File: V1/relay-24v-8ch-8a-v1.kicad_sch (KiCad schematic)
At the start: 44 parts, among them J1 DB141V-2.54-6P, J2 DB141V-2.54-6P, J3 DB142V-5.08-8P, J4 DB142V-5.08-8P, K1 G5Q-1A4-DC24V, K2 G5Q-1A4-DC24V, K3 G5Q-1A4-DC24V, K4 G5Q-1A4-DC24V, K5 G5Q-1A4-DC24V, K6 G5Q-1A4-DC24V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

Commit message: Prefab checks
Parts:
- removed J3, J4: DB142V-5.08-8P, Tales:TerminalBlock_Dibo_DB142V-5.08-8P_1x08_P5.08mm_Vertical, symbol Connector_Generic:Conn_01x08
- added J3, J4, J5, J6: DB142V-5.08-4P, Tales:TerminalBlock_Dibo_DB142V-5.08-4P_1x04_P5.08mm_Vertical, symbol Connector_Generic:Conn_01x04
- D1, D11, D13, D15, D3, D5, D7, D9: value GREEN -> EMERALD; LCSC Part # C72043 -> C2984266; Mfr Everlight -> Everlight Elec; Mfr PN 19-217/GHC-YR1S2/3T -> 19-213/GHC-XS1T1N/5T; Vendor PN C72043 -> C2984266
- J1, J2: LCSC Part # C2898747 -> C2898748; Mfr DIBO -> DORABO; Vendor PN C2898747 -> C2898748
- K1, K2, K3, K4, K5, K6, K7, K8: LCSC Part # C2931104 -> C89311; Vendor PN C2931104 -> C89311
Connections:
- net at K5.3, RV5.1: now also J5.1 (Pin_1)
- net at K5.2, RV5.2: now also J5.2 (Pin_2)
- net at K7.2, RV7.2: now also J6.2 (Pin_2)
- net at K7.3, RV7.1: now also J6.1 (Pin_1)
- net at K3.2, RV3.2: now also J4.2 (Pin_2)
- net at K3.3, RV3.1: now also J4.1 (Pin_1)
- net at K4.2, RV4.2: now also J4.4 (Pin_4)
- net at K4.3, RV4.1: now also J4.3 (Pin_3)
- net at K6.3, RV6.1: now also J5.3 (Pin_3)
- net at K6.2, RV6.2: now also J5.4 (Pin_4)
- net at K8.3, RV8.1: now also J6.3 (Pin_3)
- net at K8.2, RV8.2: now also J6.4 (Pin_4)
- net at K1.2, RV1.2: now also J3.2 (Pin_2)
- net at K1.3, RV1.1: now also J3.1 (Pin_1)
- net at K2.3, RV2.1: now also J3.3 (Pin_3)
- net at K2.2, RV2.2: now also J3.4 (Pin_4)

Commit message: Updated connectors
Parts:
- removed J1, J2: DB141V-2.54-6P, Tales:TerminalBlock_Dibo_DB141V-2.54-6P_1x06_P2.54mm_Vertical, symbol Connector_Generic:Conn_01x06
- added J1: DB141V-2.54-2P, Tales:TerminalBlock_Dibo_DB141V-2.54-2P_1x02_P2.54mm_Vertical, symbol Connector_Generic:Conn_01x02
- added J2, J3: DB141V-2.54-4P, Tales:TerminalBlock_Dibo_DB141V-2.54-4P_1x04_P2.54mm_Vertical, symbol Connector_Generic:Conn_01x04
- R1, R2, R3, R4, R5, R6, R7, R8: value 5k6/100mW -> 6k8/100mW; LCSC Part # C23189 -> C23212; Mfr PN 0603WAF5601T5E -> 0603WAF6801T5E; Vendor PN C23189 -> C23212
- renumbered J3 to J4, J4 to J5, J5 to J6, J6 to J7
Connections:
- net +24V: now also J1.1 (Pin_1), J1.2 (Pin_2)
- net at D13.1 (K), D14.2 (A), K7.5: now also J3.2 (Pin_2)
- net at D7.1 (K), D8.2 (A), K4.5: now also J2.1 (Pin_1)
- net at D5.1 (K), D6.2 (A), K3.5: now also J2.2 (Pin_2)
- net at D1.1 (K), D2.2 (A), K1.5: now also J2.4 (Pin_4)
- net at D11.1 (K), D12.2 (A), K6.5: now also J3.3 (Pin_3)
- net at D10.2 (A), D9.1 (K), K5.5: now also J3.4 (Pin_4)
- net at D15.1 (K), D16.2 (A), K8.5: now also J3.1 (Pin_1)
- net at D3.1 (K), D4.2 (A), K2.5: now also J2.3 (Pin_3)

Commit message: Review before fabrication
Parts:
- J1: LCSC Part # (none) -> C2898744; Mfr (none) -> DORABO; Mfr PN (none) -> DB141V-2.54-2P-GN; Vendor PN (none) -> C2898744
- J2, J3: LCSC Part # (none) -> C2898746; Mfr (none) -> DORABO; Mfr PN (none) -> DB141V-2.54-4P-GN; Vendor PN (none) -> C2898746
- R1, R2, R3, R4, R5, R6, R7, R8: value 6k8/100mW -> 10k/100mW; LCSC Part # C23212 -> C25804; Mfr Uniroyal -> UNI-ROYAL(Uniroyal Elec); Mfr PN 0603WAF6801T5E -> 0603WAF1002T5E; Vendor PN C23212 -> C25804
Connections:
- net IN7: now reaches D13.1 (K), D14.2 (A), J3.2 (Pin_2), K7.5
- net LED7: now reaches D13.2 (A), R7.2
- net OUT5PW: now reaches J6.1 (Pin_1), K5.3, RV5.1
- net OUT5LD: now reaches J6.2 (Pin_2), K5.2, RV5.2
- net IN4: now reaches D7.1 (K), D8.2 (A), J2.1 (Pin_1), K4.5
- net LED4: now reaches D7.2 (A), R4.2
- net OUT7LD: now reaches J7.2 (Pin_2), K7.2, RV7.2
- net OUT7PW: now reaches J7.1 (Pin_1), K7.3, RV7.1
- net OUT3LD: now reaches J5.2 (Pin_2), K3.2, RV3.2
- net OUT3PW: now reaches J5.1 (Pin_1), K3.3, RV3.1
- net IN3: now reaches D5.1 (K), D6.2 (A), J2.2 (Pin_2), K3.5
- net LED6: now reaches D11.2 (A), R6.2
- net IN8: now reaches D15.1 (K), D16.2 (A), J3.1 (Pin_1), K8.5
- net IN6: now reaches D11.1 (K), D12.2 (A), J3.3 (Pin_3), K6.5
- net IN5: now reaches D10.2 (A), D9.1 (K), J3.4 (Pin_4), K5.5
- net IN1: now reaches D1.1 (K), D2.2 (A), J2.4 (Pin_4), K1.5
- net LED8: now reaches D15.2 (A), R8.2
- net OUT6PW: now reaches J6.3 (Pin_3), K6.3, RV6.1
- net OUT6LD: now reaches J6.4 (Pin_4), K6.2, RV6.2
- net LED5: now reaches D9.2 (A), R5.2
- net LED1: now reaches D1.2 (A), R1.2
- net OUT4PW: now reaches J5.3 (Pin_3), K4.3, RV4.1
- net OUT4LD: now reaches J5.4 (Pin_4), K4.2, RV4.2
- net LED3: now reaches D5.2 (A), R3.2
- net OUT8PW: now reaches J7.3 (Pin_3), K8.3, RV8.1
- net OUT8LD: now reaches J7.4 (Pin_4), K8.2, RV8.2
- net OUT1LD: now reaches J4.2 (Pin_2), K1.2, RV1.2
- net OUT1PW: now reaches J4.1 (Pin_1), K1.3, RV1.1
- net IN2: now reaches D3.1 (K), D4.2 (A), J2.3 (Pin_3), K2.5
- net OUT2PW: now reaches J4.3 (Pin_3), K2.3, RV2.1
- net OUT2LD: now reaches J4.4 (Pin_4), K2.2, RV2.2
- net LED2: now reaches D3.2 (A), R2.2
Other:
- moved on the sheet: D1, D11, D13, D15, D3, D5, D7, D9

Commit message: Revising before manufacturing.
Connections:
- net OUT1PW renamed OUT1LN
- net OUT2PW renamed OUT2LN
- net OUT3PW renamed OUT3LN
- net OUT4PW renamed OUT4LN
- net OUT5PW renamed OUT5LN
- net OUT6PW renamed OUT6LN
- net OUT7PW renamed OUT7LN
- net OUT8PW renamed OUT8LN
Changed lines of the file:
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@@
 		)
 	)
-	(label "OUT6PW"
+	(label "OUT6LN"
 		(at 245.11 97.79 0)
 		(effects
@@
 		)
 	)
-	(label "OUT7PW"
+	(label "OUT7LN"
 		(at 245.11 130.81 0)
 		(effects
@@
 		)
 	)
-	(label "OUT8PW"
+	(label "OUT8LN"
 		(at 245.11 135.89 0)
 		(effects
@@
 		)
 	)
-	(label "OUT2PW"
+	(label "OUT2LN"
 		(at 245.11 21.59 0)
 		(effects
@@
 		)
 	)
-	(label "OUT1PW"
+	(label "OUT1LN"
 		(at 245.11 16.51 0)
 		(effects
@@
 		)
 	)
-	(label "OUT3PW"
+	(label "OUT3LN"
 		(at 245.11 54.61 0)
 		(effects
@@
 		)
 	)
-	(label "OUT4PW"
+	(label "OUT4LN"
 		(at 245.11 59.69 0)
 		(effects
@@
 		)
 	)
-	(label "OUT5PW"
+	(label "OUT5LN"
 		(at 245.11 92.71 0)
 		(effects

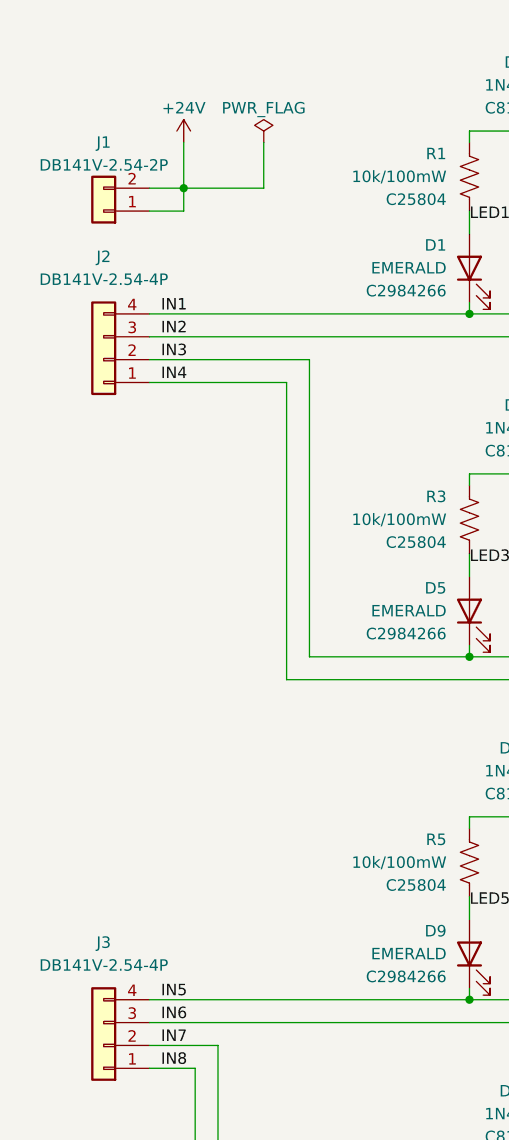
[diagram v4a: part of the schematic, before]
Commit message: Replaced input terminal blocks for 3.5mm pitch.
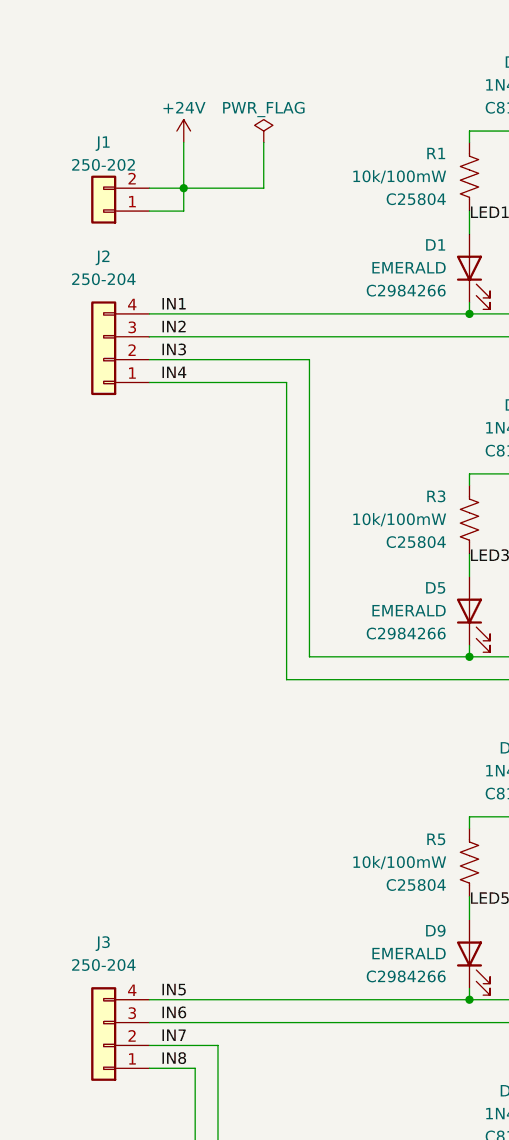
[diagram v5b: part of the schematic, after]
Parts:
- J1: value DB141V-2.54-2P -> 250-202; footprint Tales:TerminalBlock_Dibo_DB141V-2.54-2P_1x02_P2.54mm_Vertical -> Tales:TerminalBlock_Wago_250-202_1x02_P3.5mm_45Degree; LCSC Part # C2898744 -> C2765061; Mfr DORABO -> Wago; Mfr PN DB141V-2.54-2P-GN -> 250-202; Vendor PN C2898744 -> C2765061
- J2, J3: value DB141V-2.54-4P -> 250-204; footprint Tales:TerminalBlock_Dibo_DB141V-2.54-4P_1x04_P2.54mm_Vertical -> Tales:TerminalBlock_Wago_250-204_1x04_P3.5mm_45Degree; LCSC Part # C2898746 -> C2765063; Mfr DORABO -> Wago; Mfr PN DB141V-2.54-4P-GN -> 250-204; Vendor PN C2898746 -> C2765063
